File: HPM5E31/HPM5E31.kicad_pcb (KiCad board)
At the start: 4 copper layers, 70 x 50 mm, 111 parts, among them J1 USB_C_Receptacle_USB2.0_16P, J2 3220-10-0100-00, J3 RJ45_Hanrun_HR911105A_Horizon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, J4 RJ45_Hanrun_HR911105A_Horizon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, U1 HPM5E31IPB1, U2 TPS74401_VQFN, U3 JL1111-N032I, U4 JL1111-N032I, Y1 24Mhz

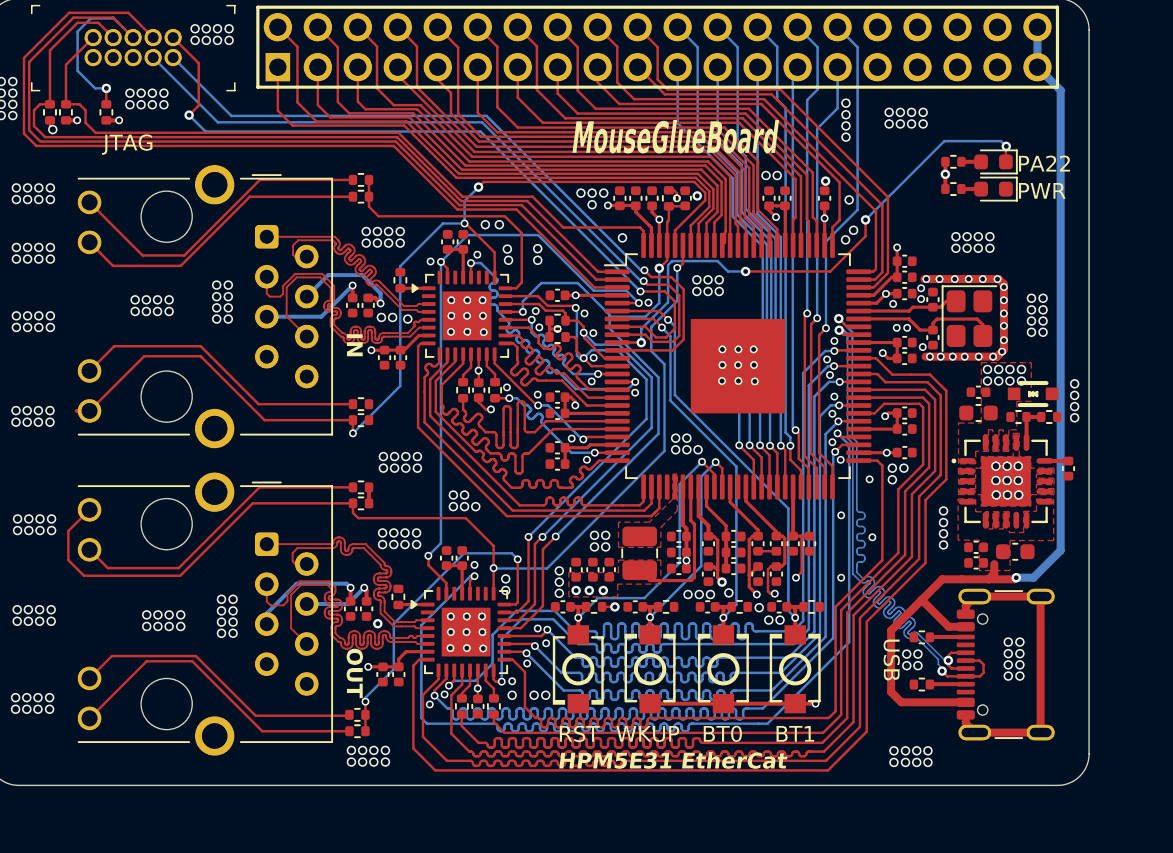
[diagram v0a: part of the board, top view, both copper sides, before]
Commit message: feat:更新HPM5E31_V0.1版本（增加缝合孔）
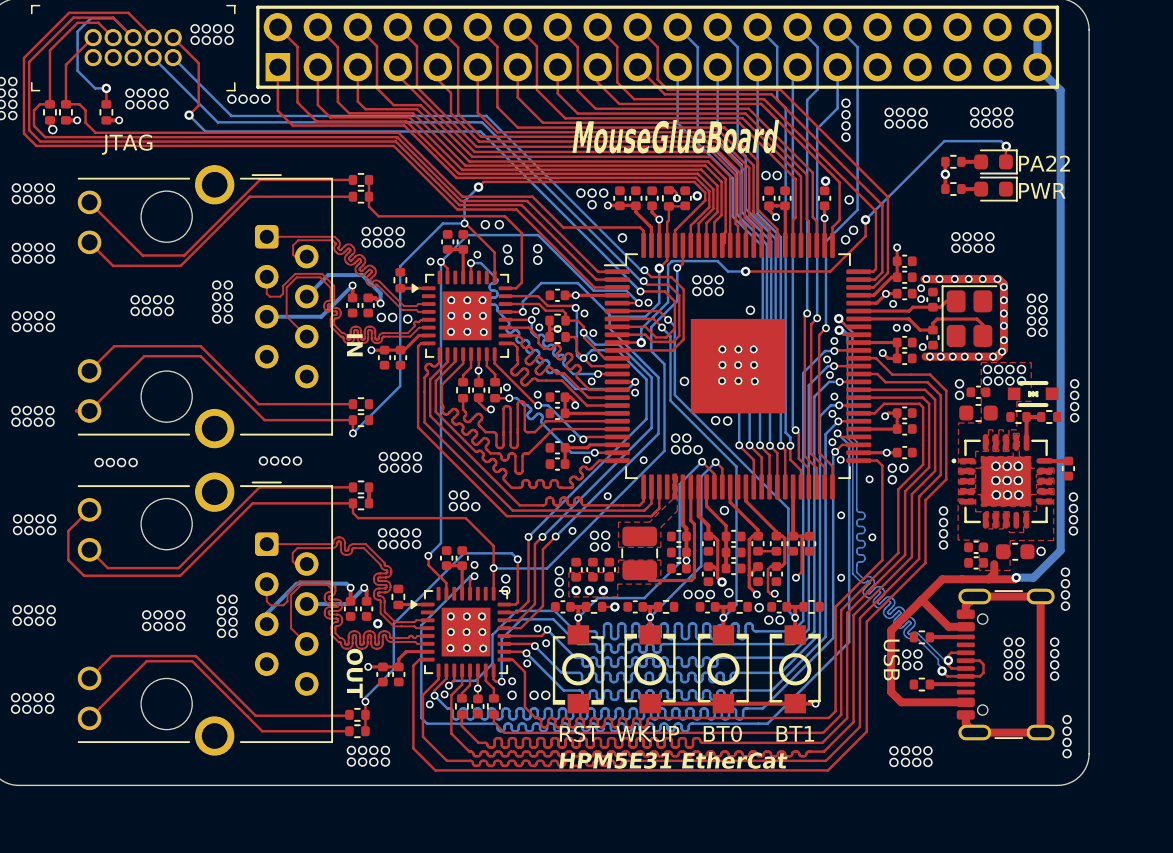
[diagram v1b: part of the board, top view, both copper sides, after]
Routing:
- net GND: vias 354 -> 401

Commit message: feat:修改HPM5E31 SOC电源供电
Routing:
- net /POWER/DCDC_SNS: track 88.8 -> 25.0 mm
- added copper zone on In2.Cu, net /POWER/DCDC_SNS
